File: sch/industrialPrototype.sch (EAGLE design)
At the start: 8 parts, among them IC1 LD1117V33C, U1 PIC16F1825-I/SL

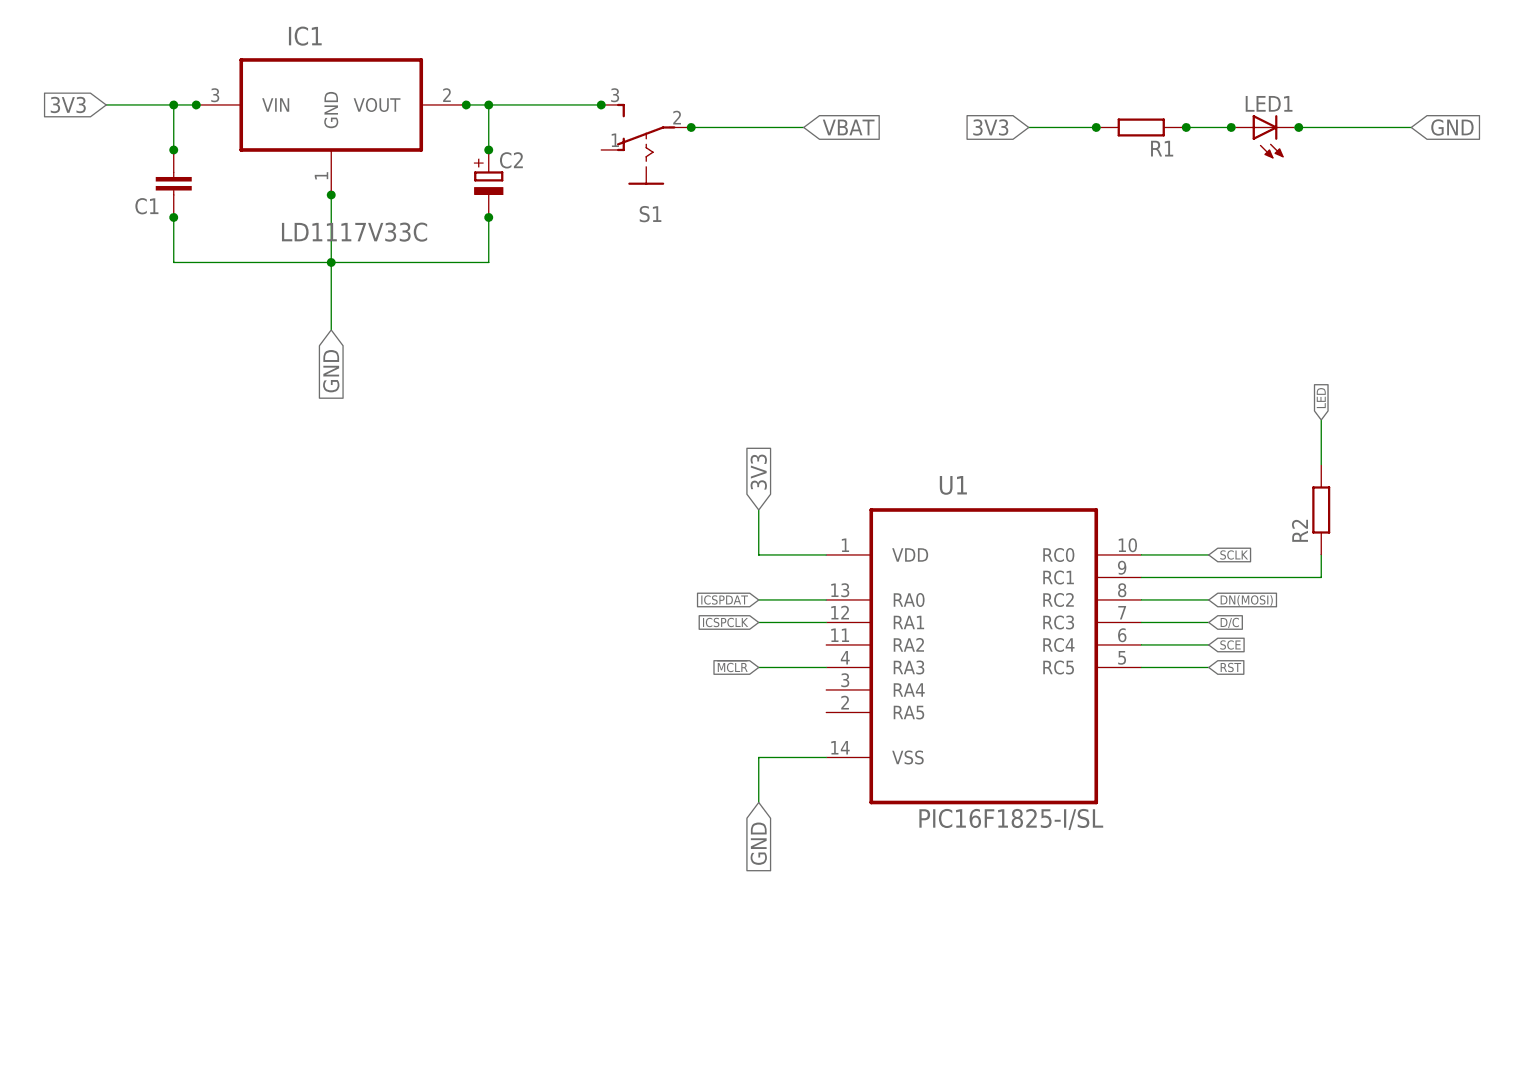
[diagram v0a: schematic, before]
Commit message: Schematic almost finished. Only temp sensor header missing
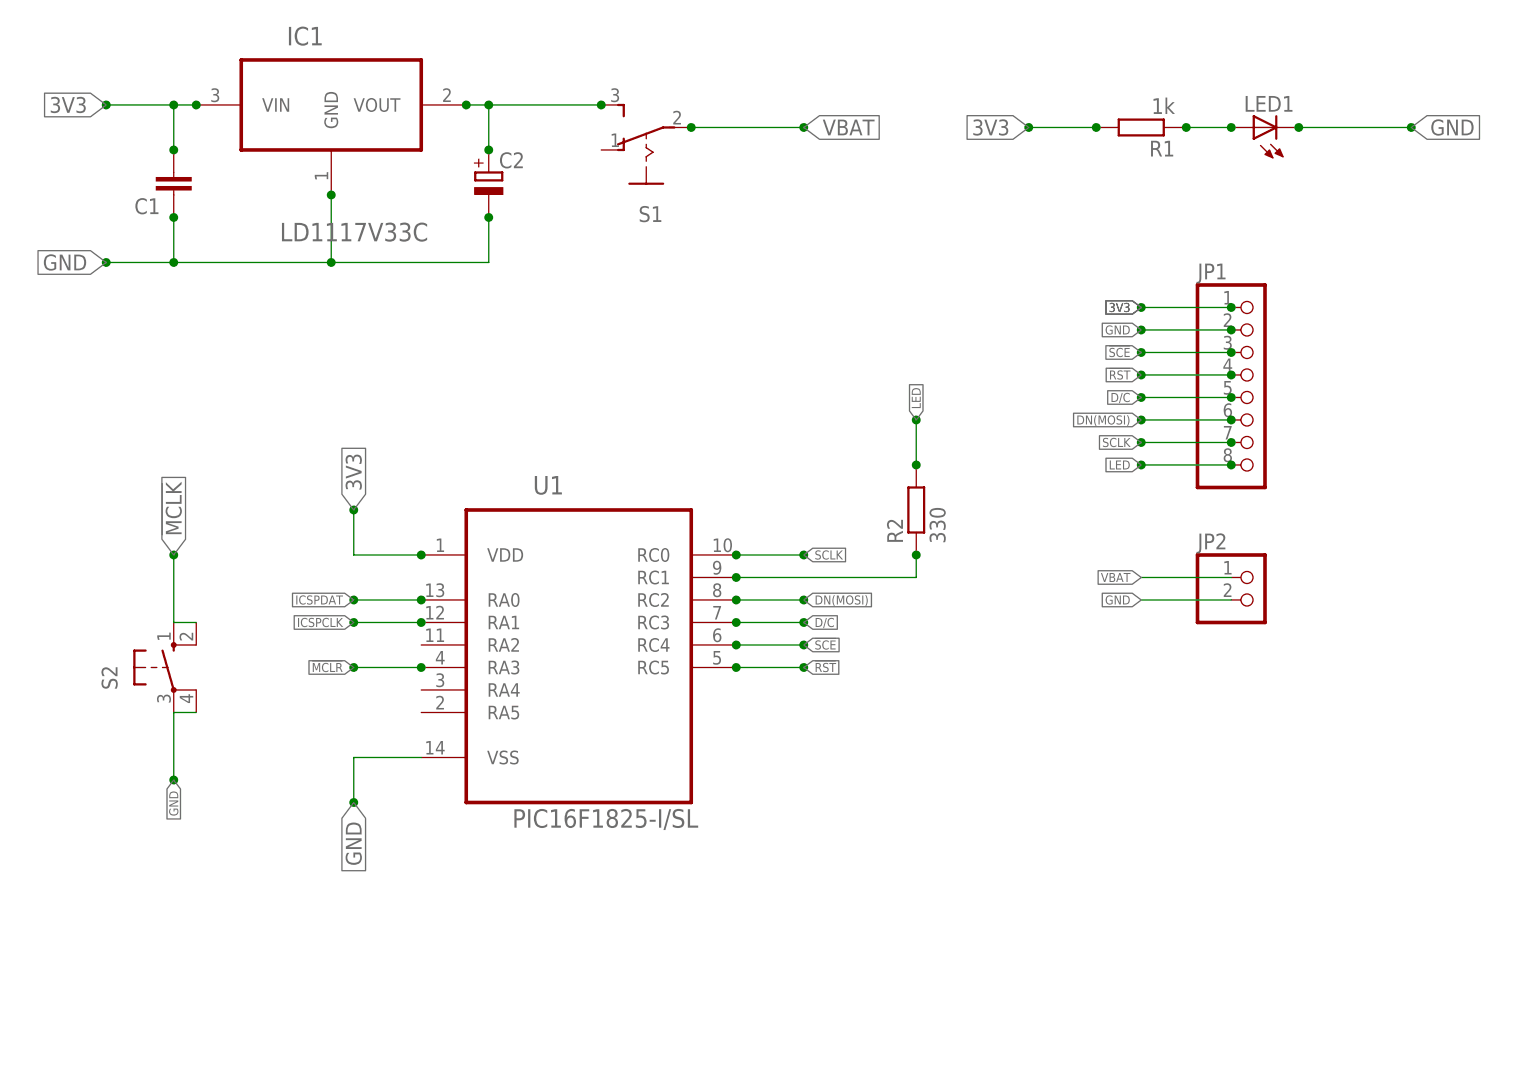
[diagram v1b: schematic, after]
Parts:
- added JP1: (no value), pinhead:PINHD-1X8
- added JP2: (no value), pinhead:PINHD-1X2
- added S2: (no value), switch-omron:10-XX
- R1: value (none) -> 1k
- R2: value (none) -> 330
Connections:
- removed net RST: U1.RC5
- removed net SCE: U1.RC4
- new net !MCLK!: S2.S, S2.S1
- new net !RST!: JP1.4, U1.RC5
- new net !SCE!: JP1.3, U1.RC4
- net 3V3: now also JP1.1
- net D/C: now also JP1.5
- net DN(MOSI): now also JP1.6
- net GND: now also JP1.2, JP2.2, S2.P, S2.P1
- net LED: now also JP1.8
- net SCLK: now also JP1.7
- net VBAT: now also JP2.1
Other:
- moved on the sheet: R2, U1

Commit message: Added Programming Header. Placed components on PCB. Routing still has to be done
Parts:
- added JP3: (no value), pinhead:PINHD-1X5
- C1: value (none) -> 47n
- C2: value (none) -> 47u
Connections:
- net !MCLR!: now also JP3.1
- net 3V3: now also JP3.2
- net GND: now also JP3.3
- net ICSPCLK: now also JP3.5
- net ICSPDAT: now also JP3.4
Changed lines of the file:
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@@
 <part name="U1" library="pic16f1825" deviceset="PIC16F1825-I/SL" device=""/>
 <part name="IC1" library="ld1117" deviceset="LD1117V33C" device=""/>
-<part name="C1" library="rcl" deviceset="C-EU" device="025-025X050"/>
-<part name="C2" library="rcl" deviceset="CPOL-EU" device="E2.5-6"/>
+<part name="C1" library="rcl" deviceset="C-EU" device="025-025X050" value="47n"/>
+<part name="C2" library="rcl" deviceset="CPOL-EU" device="E2.5-6" value="47u"/>
 <part name="S1" library="switch" deviceset="255SB" device=""/>
 <part name="LED1" library="led" deviceset="LED" device="3MM"/>
@@
 <part name="JP1" library="pinhead" deviceset="PINHD-1X8" device=""/>
 <part name="JP2" library="pinhead" deviceset="PINHD-1X2" device=""/>
+<part name="JP3" library="pinhead" deviceset="PINHD-1X5" device=""/>
 </parts>
 <sheets>
@@
 <instance part="JP1" gate="A" x="104.14" y="53.34"/>
 <instance part="JP2" gate="G$1" x="104.14" y="30.48"/>
+<instance part="JP3" gate="A" x="104.14" y="12.7"/>
 </instances>
 <busses>
@@
 <junction x="91.44" y="63.5"/>
 <junction x="101.6" y="63.5"/>
+</segment>
+<segment>
+<pinref part="JP3" gate="A" pin="2"/>
+<wire x1="101.6" y1="15.24" x2="91.44" y2="15.24" width="0.1524" layer="91"/>
+<label x="91.44" y="15.24" size="1.016" layer="95" rot="R180" xref="yes"/>
+<junction x="91.44" y="15.24"/>
+<junction x="101.6" y="15.24"/>
 </segment>
 </net>
@@
 <wire x1="101.6" y1="30.48" x2="91.44" y2="30.48" width="0.1524" layer="91"/>
 <label x="91.44" y="30.48" size="1.016" layer="95" rot="R180" xref="yes"/>
+<junction x="91.44" y="30.48"/>
+<junction x="101.6" y="30.48"/>
+</segment>
+<segment>
+<pinref part="JP3" gate="A" pin="3"/>
+<wire x1="101.6" y1="12.7" x2="91.44" y2="12.7" width="0.1524" layer="91"/>
+<label x="91.44" y="12.7" size="1.016" layer="95" rot="R180" xref="yes"/>
+<junction x="91.44" y="12.7"/>
+<junction x="101.6" y="12.7"/>
 </segment>
 </net>
@@
 <wire x1="101.6" y1="33.02" x2="91.44" y2="33.02" width="0.1524" layer="91"/>
 <label x="91.44" y="33.02" size="1.016" layer="95" rot="R180" xref="yes"/>
+<junction x="91.44" y="33.02"/>
+<junction x="101.6" y="33.02"/>
 </segment>
 </net>
@@
 <junction x="10.16" y="22.86"/>
 </segment>
+<segment>
+<pinref part="JP3" gate="A" pin="1"/>
+<wire x1="101.6" y1="17.78" x2="91.44" y2="17.78" width="0.1524" layer="91"/>
+<label x="91.44" y="17.78" size="1.016" layer="95" rot="R180" xref="yes"/>
+<junction x="91.44" y="17.78"/>
+<junction x="101.6" y="17.78"/>
+</segment>
 </net>
 <net name="ICSPDAT" class="0">
@@
 <junction x="10.16" y="30.48"/>
 </segment>
+<segment>
+<pinref part="JP3" gate="A" pin="4"/>
+<wire x1="101.6" y1="10.16" x2="91.44" y2="10.16" width="0.1524" layer="91"/>
+<label x="91.44" y="10.16" size="1.016" layer="95" rot="R180" xref="yes"/>
+<junction x="91.44" y="10.16"/>
+<junction x="101.6" y="10.16"/>
+</segment>
 </net>
 <net name="ICSPCLK" class="0">
@@
 <junction x="10.16" y="27.94"/>
 </segment>
-</net>
+<segment>
+<pinref part="JP3" gate="A" pin="5"/>
+<wire x1="101.6" y1="7.62" x2="91.44" y2="7.62" width="0.1524" layer="91"/>
+<label x="91.44" y="7.62" size="1.016" layer="95" rot="R180" xref="yes"/>
+<junction x="91.44" y="7.62"/>
+<junction x="101.6" y="7.62"/>
+</segment>
+</net>

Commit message: Added the screen and did the auto-route. Labels still need to be fixed
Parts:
- removed JP1: (no value), pinhead:PINHD-1X8
- added U$1: NOKIA5110, CustomLib:NOKIA5110
- C2: value 47u -> 100u
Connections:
- net !RST!: now also U$1.RST-B; no longer JP1.4
- net !SCE!: now also U$1.SCE-B; no longer JP1.3
- net 3V3: now also U$1.VCC-B; no longer JP1.1
- net D/C: now also U$1.D/C-B; no longer JP1.5
- net DN(MOSI): now also U$1.DN-B; no longer JP1.6
- net GND: now also U$1.GND-B; no longer JP1.2
- net LED: now also U$1.LED-B; no longer JP1.8
- net SCLK: now also U$1.SCLK-B; no longer JP1.7
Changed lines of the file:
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@@
 <part name="IC1" library="ld1117" deviceset="LD1117V33C" device=""/>
 <part name="C1" library="rcl" deviceset="C-EU" device="025-025X050" value="47n"/>
-<part name="C2" library="rcl" deviceset="CPOL-EU" device="E2.5-6" value="47u"/>
+<part name="C2" library="rcl" deviceset="CPOL-EU" device="E2.5-6" value="100u"/>
 <part name="S1" library="switch" deviceset="255SB" device=""/>
 <part name="LED1" library="led" deviceset="LED" device="3MM"/>
@@
 <part name="R2" library="resistor" deviceset="R-EU_" device="0204/5" value="330"/>
 <part name="S2" library="switch-omron" deviceset="10-XX" device=""/>
-<part name="JP1" library="pinhead" deviceset="PINHD-1X8" device=""/>
 <part name="JP2" library="pinhead" deviceset="PINHD-1X2" device=""/>
 <part name="JP3" library="pinhead" deviceset="PINHD-1X5" device=""/>
+<part name="U$1" library="CustomLib" deviceset="NOKIA5110" device=""/>
 </parts>
 <sheets>
@@
 <instance part="R2" gate="G$1" x="66.04" y="40.64" rot="R90"/>
 <instance part="S2" gate="1" x="-17.78" y="22.86"/>
-<instance part="JP1" gate="A" x="104.14" y="53.34"/>
 <instance part="JP2" gate="G$1" x="104.14" y="30.48"/>
 <instance part="JP3" gate="A" x="104.14" y="12.7"/>
+<instance part="U$1" gate="G$1" x="111.76" y="53.34"/>
 </instances>
 <busses>
@@
 </segment>
 <segment>
-<pinref part="JP1" gate="A" pin="1"/>
-<wire x1="101.6" y1="63.5" x2="91.44" y2="63.5" width="0.1524" layer="91"/>
 <label x="91.44" y="63.5" size="1.016" layer="95" rot="R180" xref="yes"/>
 <label x="91.44" y="63.5" size="1.016" layer="95" rot="R180" xref="yes"/>
 <junction x="91.44" y="63.5"/>
-<junction x="101.6" y="63.5"/>
+<wire x1="96.52" y1="63.5" x2="91.44" y2="63.5" width="0.1524" layer="91"/>
+<pinref part="U$1" gate="G$1" pin="VCC-B"/>
+<junction x="96.52" y="63.5"/>
 </segment>
 <segment>
@@
 </segment>
 <segment>
-<pinref part="JP1" gate="A" pin="2"/>
-<wire x1="101.6" y1="60.96" x2="91.44" y2="60.96" width="0.1524" layer="91"/>
 <label x="91.44" y="60.96" size="1.016" layer="95" rot="R180" xref="yes"/>
 <junction x="91.44" y="60.96"/>
-<junction x="101.6" y="60.96"/>
+<wire x1="96.52" y1="60.96" x2="91.44" y2="60.96" width="0.1524" layer="91"/>
+<pinref part="U$1" gate="G$1" pin="GND-B"/>
+<junction x="96.52" y="60.96"/>
 </segment>
 <segment>
@@
 </segment>
 <segment>
-<pinref part="JP1" gate="A" pin="7"/>
-<wire x1="101.6" y1="48.26" x2="91.44" y2="48.26" width="0.1524" layer="91"/>
 <label x="91.44" y="48.26" size="1.016" layer="95" rot="R180" xref="yes"/>
 <junction x="91.44" y="48.26"/>
-<junction x="101.6" y="48.26"/>
+<wire x1="96.52" y1="48.26" x2="91.44" y2="48.26" width="0.1524" layer="91"/>
+<pinref part="U$1" gate="G$1" pin="SCLK-B"/>
+<junction x="96.52" y="48.26"/>
 </segment>
 </net>
@@
 </segment>
 <segment>
-<pinref part="JP1" gate="A" pin="6"/>
-<wire x1="101.6" y1="50.8" x2="91.44" y2="50.8" width="0.1524" layer="91"/>
 <label x="91.44" y="50.8" size="1.016" layer="95" rot="R180" xref="yes"/>
 <junction x="91.44" y="50.8"/>
-<junction x="101.6" y="50.8"/>
+<wire x1="96.52" y1="50.8" x2="91.44" y2="50.8" width="0.1524" layer="91"/>
+<pinref part="U$1" gate="G$1" pin="DN-B"/>
+<junction x="96.52" y="50.8"/>
 </segment>
 </net>
@@
 </segment>
 <segment>
-<pinref part="JP1" gate="A" pin="5"/>
-<wire x1="101.6" y1="53.34" x2="91.44" y2="53.34" width="0.1524" layer="91"/>
 <label x="91.44" y="53.34" size="1.016" layer="95" rot="R180" xref="yes"/>
 <junction x="91.44" y="53.34"/>
-<junction x="101.6" y="53.34"/>
+<wire x1="96.52" y1="53.34" x2="91.44" y2="53.34" width="0.1524" layer="91"/>
+<pinref part="U$1" gate="G$1" pin="D/C-B"/>
+<junction x="96.52" y="53.34"/>
 </segment>
 </net>
@@
 </segment>
 <segment>
-<pinref part="JP1" gate="A" pin="3"/>
-<wire x1="101.6" y1="58.42" x2="91.44" y2="58.42" width="0.1524" layer="91"/>
 <label x="91.44" y="58.42" size="1.016" layer="95" rot="R180" xref="yes"/>
 <junction x="91.44" y="58.42"/>
-<junction x="101.6" y="58.42"/>
+<wire x1="96.52" y1="58.42" x2="91.44" y2="58.42" width="0.1524" layer="91"/>
+<pinref part="U$1" gate="G$1" pin="SCE-B"/>
+<junction x="96.52" y="58.42"/>
 </segment>
 </net>
@@
 </segment>
 <segment>
-<pinref part="JP1" gate="A" pin="4"/>
-<wire x1="101.6" y1="55.88" x2="91.44" y2="55.88" width="0.1524" layer="91"/>
 <label x="91.44" y="55.88" size="1.016" layer="95" rot="R180" xref="yes"/>
 <junction x="91.44" y="55.88"/>
-<junction x="101.6" y="55.88"/>
+<wire x1="96.52" y1="55.88" x2="91.44" y2="55.88" width="0.1524" layer="91"/>
+<pinref part="U$1" gate="G$1" pin="RST-B"/>
+<junction x="96.52" y="55.88"/>
 </segment>
 </net>
@@
 </segment>
 <segment>
-<pinref part="JP1" gate="A" pin="8"/>
-<wire x1="101.6" y1="45.72" x2="91.44" y2="45.72" width="0.1524" layer="91"/>
 <label x="91.44" y="45.72" size="1.016" layer="95" rot="R180" xref="yes"/>
 <junction x="91.44" y="45.72"/>
-<junction x="101.6" y="45.72"/>
-</segment>
-</net>
+<wire x1="96.52" y1="45.72" x2="91.44" y2="45.72" width="0.1524" layer="91"/>
+<pinref part="U$1" gate="G$1" pin="LED-B"/>
+<junction x="96.52" y="45.72"/>
+</segment>
+</net>

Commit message: Added the Temperature Sensor Socket
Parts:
- added JP1: (no value), pinhead:PINHD-1X3
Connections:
- new net 1WIRE_DS18B20: JP1.3, U1.RA2
- net 3V3: now also JP1.1
- net GND: now also JP1.2
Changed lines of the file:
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@@
 <part name="JP3" library="pinhead" deviceset="PINHD-1X5" device=""/>
 <part name="U$1" library="CustomLib" deviceset="NOKIA5110" device=""/>
+<part name="JP1" library="pinhead" deviceset="PINHD-1X3" device=""/>
 </parts>
 <sheets>
@@
 <instance part="JP3" gate="A" x="104.14" y="12.7"/>
 <instance part="U$1" gate="G$1" x="111.76" y="53.34"/>
+<instance part="JP1" gate="A" x="104.14" y="-5.08"/>
 </instances>
 <busses>
@@
 <junction x="91.44" y="15.24"/>
 <junction x="101.6" y="15.24"/>
+</segment>
+<segment>
+<pinref part="JP1" gate="A" pin="1"/>
+<wire x1="101.6" y1="-2.54" x2="91.44" y2="-2.54" width="0.1524" layer="91"/>
+<label x="91.44" y="-2.54" size="1.016" layer="95" rot="R180" xref="yes"/>
 </segment>
 </net>
@@
 <junction x="101.6" y="12.7"/>
 </segment>
+<segment>
+<pinref part="JP1" gate="A" pin="2"/>
+<wire x1="101.6" y1="-5.08" x2="91.44" y2="-5.08" width="0.1524" layer="91"/>
+<label x="91.44" y="-5.08" size="1.016" layer="95" rot="R180" xref="yes"/>
+</segment>
 </net>
 <net name="VBAT" class="0">
@@
 </segment>
 </net>
+<net name="1WIRE_DS18B20" class="0">
+<segment>
+<pinref part="U1" gate="A" pin="RA2"/>
+<wire x1="10.16" y1="25.4" x2="2.54" y2="25.4" width="0.1524" layer="91"/>
+<label x="2.54" y="25.4" size="1.016" layer="95" rot="R180" xref="yes"/>
+<junction x="2.54" y="25.4"/>
+</segment>
+<segment>
+<pinref part="JP1" gate="A" pin="3"/>
+<wire x1="101.6" y1="-7.62" x2="91.44" y2="-7.62" width="0.1524" layer="91"/>
+<label x="91.44" y="-7.62" size="1.016" layer="95" rot="R180" xref="yes"/>
+</segment>
+</net>

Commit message: Final Version of the Schematic and Board
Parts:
- removed U$1: NOKIA5110, CustomLib:NOKIA5110
- added NOKIA5110: NOKIA5110, CustomLib:NOKIA5110
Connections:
- net !RST!: now also NOKIA5110.RST-B; no longer U$1.RST-B
- net !SCE!: now also NOKIA5110.SCE-B; no longer U$1.SCE-B
- net 3V3: now also NOKIA5110.VCC-B; no longer U$1.VCC-B
- net D/C: now also NOKIA5110.D/C-B; no longer U$1.D/C-B
- net DN(MOSI): now also NOKIA5110.DN-B; no longer U$1.DN-B
- net GND: now also NOKIA5110.GND-B; no longer U$1.GND-B
- net LED: now also NOKIA5110.LED-B; no longer U$1.LED-B
- net SCLK: now also NOKIA5110.SCLK-B; no longer U$1.SCLK-B
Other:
- moved on the sheet: C1, C2, IC1, JP1, JP2, JP3, LED1, R1, R2, S1, S2, U1
